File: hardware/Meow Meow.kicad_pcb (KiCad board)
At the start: 2 copper layers, 73.1 x 45.2 mm, 40 parts, among them J1 USB_B_Micro, J2 SWD, P1 SPACE, P10 A, P11 W, P12 KEY_UP_ARROW, P2 KEY_DOWN_ARROW, P3 KEY_RIGHT_ARROW, P5 KEY_LEFT_ARROW, P6 D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

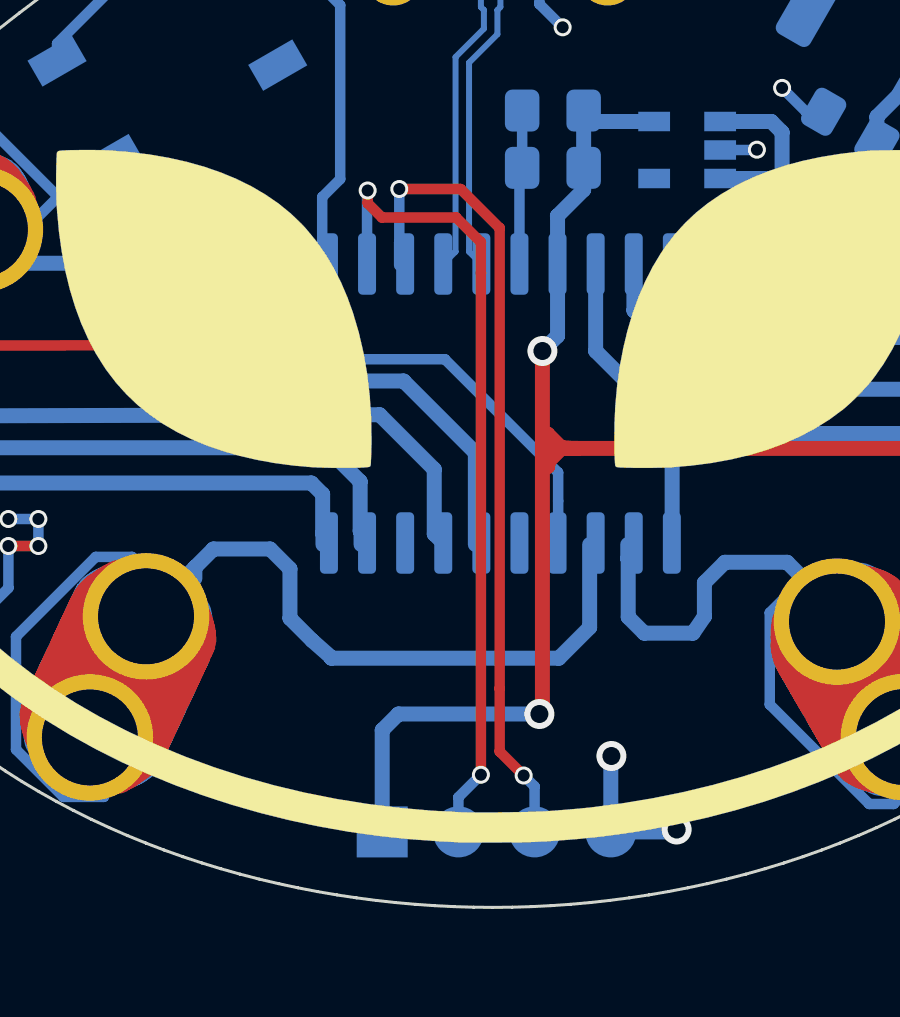
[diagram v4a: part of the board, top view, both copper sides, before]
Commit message: swd port change
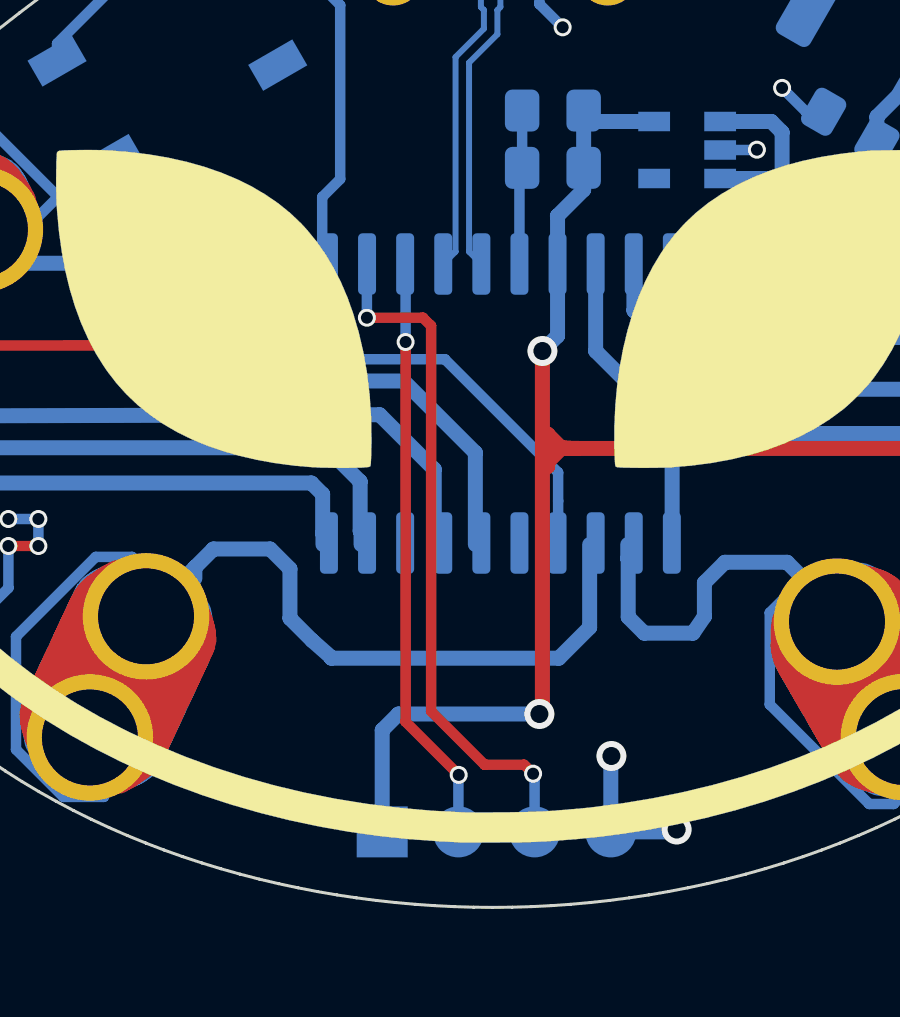
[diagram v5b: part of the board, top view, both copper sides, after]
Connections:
- J2 pad 2: /SWCLK -> /SWDIO
- J2 pad 3: /SWDIO -> /SWCLK
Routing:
- net /SWDIO: track 27.0 -> 19.7 mm
- net /SWCLK: track 27.2 -> 23.1 mm
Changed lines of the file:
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@@
-(kicad_pcb (version 20171130) (host pcbnew "(5.1.5-0-10_14)")
+(kicad_pcb (version 20171130) (host pcbnew "(5.1.4-0-10_14)")
   (general
     (thickness 1.6)
     (drawings 5)
-    (tracks 317)
+    (tracks 313)
     (zones 0)
     (modules 40)
@@
     (32 B.Adhes user)
     (33 F.Adhes user)
-    (34 B.Paste user)
+    (34 B.Paste user hide)
     (35 F.Paste user)
     (36 B.SilkS user)
-    (37 F.SilkS user)
+    (37 F.SilkS user hide)
     (38 B.Mask user)
     (39 F.Mask user)
@@
       (net 1 GND))
     (pad 3 smd oval (at 0 -5.08 270) (size 1.7 1.7) (layers B.Cu B.Paste B.Mask)
-      (net 4 /SWDIO))
-    (pad 2 smd oval (at 0 -2.54 270) (size 1.7 1.7) (layers B.Cu B.Paste B.Mask)
       (net 7 /SWCLK))
+    (pad 2 smd oval (at 0 -2.54 270) (size 1.7 1.7) (layers B.Cu B.Paste B.Mask)
+      (net 4 /SWDIO))
     (pad 1 smd rect (at 0 0 270) (size 1.7 1.7) (layers B.Cu B.Paste B.Mask)
       (net 3 +3V3))
@@
   (segment (start 162.147446 115.647446) (end 145.147446 115.647446) (width 0.5) (layer F.Cu) (net 3))
   (segment (start 163.6 117.1) (end 162.147446 115.647446) (width 0.5) (layer F.Cu) (net 3))
-  (via (at 143.575 126.55) (size 0.6) (drill 0.4) (layers F.Cu B.Cu) (net 4))
-  (segment (start 143.94 126.915) (end 143.575 126.55) (width 0.35) (layer B.Cu) (net 4))
-  (segment (start 143.94 128.43) (end 143.94 126.915) (width 0.35) (layer B.Cu) (net 4))
-  (segment (start 139.425 109.55) (end 139.425 108.785) (width 0.35) (layer B.Cu) (net 4))
-  (segment (start 139.43 108.78) (end 139.43 107) (width 0.35) (layer B.Cu) (net 4))
-  (segment (start 139.425 108.785) (end 139.43 108.78) (width 0.35) (layer B.Cu) (net 4))
-  (via (at 139.43 107) (size 0.6) (drill 0.4) (layers F.Cu B.Cu) (net 4))
-  (segment (start 141.475 107) (end 142.775 108.3) (width 0.35) (layer F.Cu) (net 4))
-  (segment (start 139.43 107) (end 141.475 107) (width 0.35) (layer F.Cu) (net 4))
-  (segment (start 142.775 125.75) (end 143.575 126.55) (width 0.35) (layer F.Cu) (net 4))
-  (segment (start 142.775 123.65) (end 142.775 125.75) (width 0.35) (layer F.Cu) (net 4))
-  (segment (start 142.775 108.3) (end 142.775 123.65) (width 0.35) (layer F.Cu) (net 4))
+  (via (at 141.41 126.53) (size 0.6) (drill 0.4) (layers F.Cu B.Cu) (net 4))
+  (segment (start 141.4 126.54) (end 141.41 126.53) (width 0.35) (layer B.Cu) (net 4))
+  (segment (start 141.4 128.43) (end 141.4 126.54) (width 0.35) (layer B.Cu) (net 4))
+  (segment (start 139.64 124.76) (end 139.64 112.1) (width 0.35) (layer F.Cu) (net 4))
+  (via (at 139.64 112.1) (size 0.6) (drill 0.4) (layers F.Cu B.Cu) (net 4))
+  (segment (start 141.41 126.53) (end 139.64 124.76) (width 0.35) (layer F.Cu) (net 4))
+  (segment (start 139.64 109.515) (end 139.625 109.5) (width 0.35) (layer B.Cu) (net 4))
+  (segment (start 139.64 112.1) (end 139.64 109.515) (width 0.35) (layer B.Cu) (net 4))
   (segment (start 141.305 109.09) (end 140.895 109.5) (width 0.2) (layer B.Cu) (net 5))
   (segment (start 142.25 101.6568) (end 141.305 102.6018) (width 0.2) (layer B.Cu) (net 5))
@@
   (segment (start 142.7 101.035001) (end 142.7 101.8432) (width 0.2) (layer B.Cu) (net 6))
   (segment (start 142.8 100.935001) (end 142.7 101.035001) (width 0.2) (layer B.Cu) (net 6))
-  (segment (start 141.4 127.275) (end 142.15 126.525) (width 0.35) (layer B.Cu) (net 7))
-  (segment (start 141.4 128.43) (end 141.4 127.275) (width 0.35) (layer B.Cu) (net 7))
-  (via (at 142.15 126.525) (size 0.6) (drill 0.4) (layers F.Cu B.Cu) (net 7))
-  (segment (start 142.15 126.525) (end 142.15 109.8) (width 0.35) (layer F.Cu) (net 7))
-  (via (at 138.375 107.05) (size 0.6) (drill 0.4) (layers F.Cu B.Cu) (net 7))
-  (segment (start 138.355 107.07) (end 138.375 107.05) (width 0.35) (layer B.Cu) (net 7))
-  (segment (start 138.355 109.5) (end 138.355 107.07) (width 0.35) (layer B.Cu) (net 7))
-  (segment (start 138.375 107.474264) (end 138.850736 107.95) (width 0.35) (layer F.Cu) (net 7))
-  (segment (start 138.375 107.05) (end 138.375 107.474264) (width 0.35) (layer F.Cu) (net 7))
-  (segment (start 138.850736 107.95) (end 141.325 107.95) (width 0.35) (layer F.Cu) (net 7))
-  (segment (start 142.15 108.775) (end 142.15 109.8) (width 0.35) (layer F.Cu) (net 7))
-  (segment (start 141.325 107.95) (end 142.15 108.775) (width 0.35) (layer F.Cu) (net 7))
+  (segment (start 143.94 126.54) (end 143.89 126.49) (width 0.35) (layer B.Cu) (net 7))
+  (via (at 143.89 126.49) (size 0.6) (drill 0.4) (layers F.Cu B.Cu) (net 7))
+  (segment (start 143.94 128.43) (end 143.94 126.54) (width 0.35) (layer B.Cu) (net 7))
+  (segment (start 143.590001 126.190001) (end 142.270001 126.190001) (width 0.35) (layer F.Cu) (net 7))
+  (segment (start 143.89 126.49) (end 143.590001 126.190001) (width 0.35) (layer F.Cu) (net 7))
+  (segment (start 142.270001 126.190001) (end 140.49 124.41) (width 0.35) (layer F.Cu) (net 7))
+  (segment (start 140.49 124.41) (end 140.49 111.56) (width 0.35) (layer F.Cu) (net 7))
+  (via (at 138.35 111.29) (size 0.6) (drill 0.4) (layers F.Cu B.Cu) (net 7))
+  (segment (start 140.22 111.29) (end 138.35 111.29) (width 0.35) (layer F.Cu) (net 7))
+  (segment (start 140.49 111.56) (end 140.22 111.29) (width 0.35) (layer F.Cu) (net 7))
+  (segment (start 138.35 109.505) (end 138.355 109.5) (width 0.35) (layer B.Cu) (net 7))
+  (segment (start 138.35 111.29) (end 138.35 109.505) (width 0.35) (layer B.Cu) (net 7))
   (segment (start 116.325 115.625) (end 115.275 116.675) (width 0.5) (layer B.Cu) (net 8))
   (segment (start 137 115.625) (end 116.325 115.625) (width 0.5) (layer B.Cu) (net 8))

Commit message: correct swd port change
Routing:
- net /SWCLK: track 23.1 -> 29.1 mm
- net /SWDIO: track 19.7 -> 24.6 mm
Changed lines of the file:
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@@
     (thickness 1.6)
     (drawings 5)
-    (tracks 313)
+    (tracks 316)
     (zones 0)
     (modules 40)
@@
   (segment (start 141.4 126.54) (end 141.41 126.53) (width 0.35) (layer B.Cu) (net 4))
   (segment (start 141.4 128.43) (end 141.4 126.54) (width 0.35) (layer B.Cu) (net 4))
-  (segment (start 139.64 124.76) (end 139.64 112.1) (width 0.35) (layer F.Cu) (net 4))
-  (via (at 139.64 112.1) (size 0.6) (drill 0.4) (layers F.Cu B.Cu) (net 4))
-  (segment (start 141.41 126.53) (end 139.64 124.76) (width 0.35) (layer F.Cu) (net 4))
-  (segment (start 139.64 109.515) (end 139.625 109.5) (width 0.35) (layer B.Cu) (net 4))
-  (segment (start 139.64 112.1) (end 139.64 109.515) (width 0.35) (layer B.Cu) (net 4))
+  (segment (start 141.41 126.53) (end 141.41 107.84) (width 0.35) (layer F.Cu) (net 4))
+  (segment (start 141.41 107.84) (end 140.87 107.3) (width 0.35) (layer F.Cu) (net 4))
+  (via (at 139.63 107.59) (size 0.6) (drill 0.4) (layers F.Cu B.Cu) (net 4))
+  (segment (start 139.92 107.3) (end 139.63 107.59) (width 0.35) (layer F.Cu) (net 4))
+  (segment (start 140.87 107.3) (end 139.92 107.3) (width 0.35) (layer F.Cu) (net 4))
+  (segment (start 139.63 109.495) (end 139.625 109.5) (width 0.35) (layer B.Cu) (net 4))
+  (segment (start 139.63 107.59) (end 139.63 109.495) (width 0.35) (layer B.Cu) (net 4))
   (segment (start 141.305 109.09) (end 140.895 109.5) (width 0.2) (layer B.Cu) (net 5))
   (segment (start 142.25 101.6568) (end 141.305 102.6018) (width 0.2) (layer B.Cu) (net 5))
@@
   (via (at 143.89 126.49) (size 0.6) (drill 0.4) (layers F.Cu B.Cu) (net 7))
   (segment (start 143.94 128.43) (end 143.94 126.54) (width 0.35) (layer B.Cu) (net 7))
-  (segment (start 143.590001 126.190001) (end 142.270001 126.190001) (width 0.35) (layer F.Cu) (net 7))
-  (segment (start 143.89 126.49) (end 143.590001 126.190001) (width 0.35) (layer F.Cu) (net 7))
-  (segment (start 142.270001 126.190001) (end 140.49 124.41) (width 0.35) (layer F.Cu) (net 7))
-  (segment (start 140.49 124.41) (end 140.49 111.56) (width 0.35) (layer F.Cu) (net 7))
-  (via (at 138.35 111.29) (size 0.6) (drill 0.4) (layers F.Cu B.Cu) (net 7))
-  (segment (start 140.22 111.29) (end 138.35 111.29) (width 0.35) (layer F.Cu) (net 7))
-  (segment (start 140.49 111.56) (end 140.22 111.29) (width 0.35) (layer F.Cu) (net 7))
-  (segment (start 138.35 109.505) (end 138.355 109.5) (width 0.35) (layer B.Cu) (net 7))
-  (segment (start 138.35 111.29) (end 138.35 109.505) (width 0.35) (layer B.Cu) (net 7))
+  (via (at 138.34 107.79) (size 0.6) (drill 0.4) (layers F.Cu B.Cu) (net 7))
+  (segment (start 138.34 109.485) (end 138.355 109.5) (width 0.35) (layer B.Cu) (net 7))
+  (segment (start 138.34 107.79) (end 138.34 109.485) (width 0.35) (layer B.Cu) (net 7))
+  (segment (start 138.8 106.59) (end 138.34 107.05) (width 0.35) (layer F.Cu) (net 7))
+  (segment (start 141.42 106.59) (end 138.8 106.59) (width 0.35) (layer F.Cu) (net 7))
+  (segment (start 138.34 107.05) (end 138.34 107.79) (width 0.35) (layer F.Cu) (net 7))
+  (segment (start 142.42 107.59) (end 141.42 106.59) (width 0.35) (layer F.Cu) (net 7))
+  (segment (start 143.1 126.49) (end 142.42 125.81) (width 0.35) (layer F.Cu) (net 7))
+  (segment (start 143.89 126.49) (end 143.1 126.49) (width 0.35) (layer F.Cu) (net 7))
+  (segment (start 142.42 125.81) (end 142.42 107.59) (width 0.35) (layer F.Cu) (net 7))
   (segment (start 116.325 115.625) (end 115.275 116.675) (width 0.5) (layer B.Cu) (net 8))
   (segment (start 137 115.625) (end 116.325 115.625) (width 0.5) (layer B.Cu) (net 8))
